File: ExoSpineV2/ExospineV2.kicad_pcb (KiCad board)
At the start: 2 copper layers, 79.2 x 75.6 mm, 51 parts, among them J1 GPIO, J11 JST PH 3pin, J12 2.54mm 4pin, J13 JST PH 5pin, J2 Screw Terminal 2pin 5mm, J21 JST PH 2pin, J22 JST PH 2pin, J23 JST PH 2pin, J3 Mounting Hole 2.7mm, J31 JST PH 3pin, J32 JST PH 3pin, J33 JST PH 3pin, J34 JST PH 3pin, J35 JST PH 3pin, J36 JST PH 3pin, J4 Mounting Hole 2.7mm, J5 Mounting Hole 2.7mm, J51 JST PH 2pin, J6 Mounting Hole 2.7mm, J61 JST PH 2pin, J71 JST PH 4pin, J72 JST PH 3pin, J73 JST PH 4pin, J74 JST PH 3pin, J75 JST PH 4pin, J76 JST PH 3pin, J77 JST PH 4pin, J78 JST PH 3pin, J81 JST PH 3pin, J82 JST PH 3pin, U1 MCP3008-I/SL, U2 74HC00D,653, U3 74HC00D,653

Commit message: little modifications
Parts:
- moved D1 5.30 mm to (117.3, 21.7)
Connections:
- J1 pad 12: /TemperatureSensors -> /Battery.NALCC
- J1 pad 7: /Battery.NALCC -> /TemperatureSensors
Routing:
- net Net-(J2-Pin_1): track 11.3 -> 0.00 mm
- net /Battery.NALCC: track 19.6 -> 28.6 mm
- net /Actuator2.Feedback: track 56.4 -> 61.0 mm, vias 0 -> 2
- net /TemperatureSensors: track 54.0 -> 52.4 mm
- added copper zone on B.Cu, net +5V
- added copper zone on F.Cu, net Net-(J2-Pin_1)

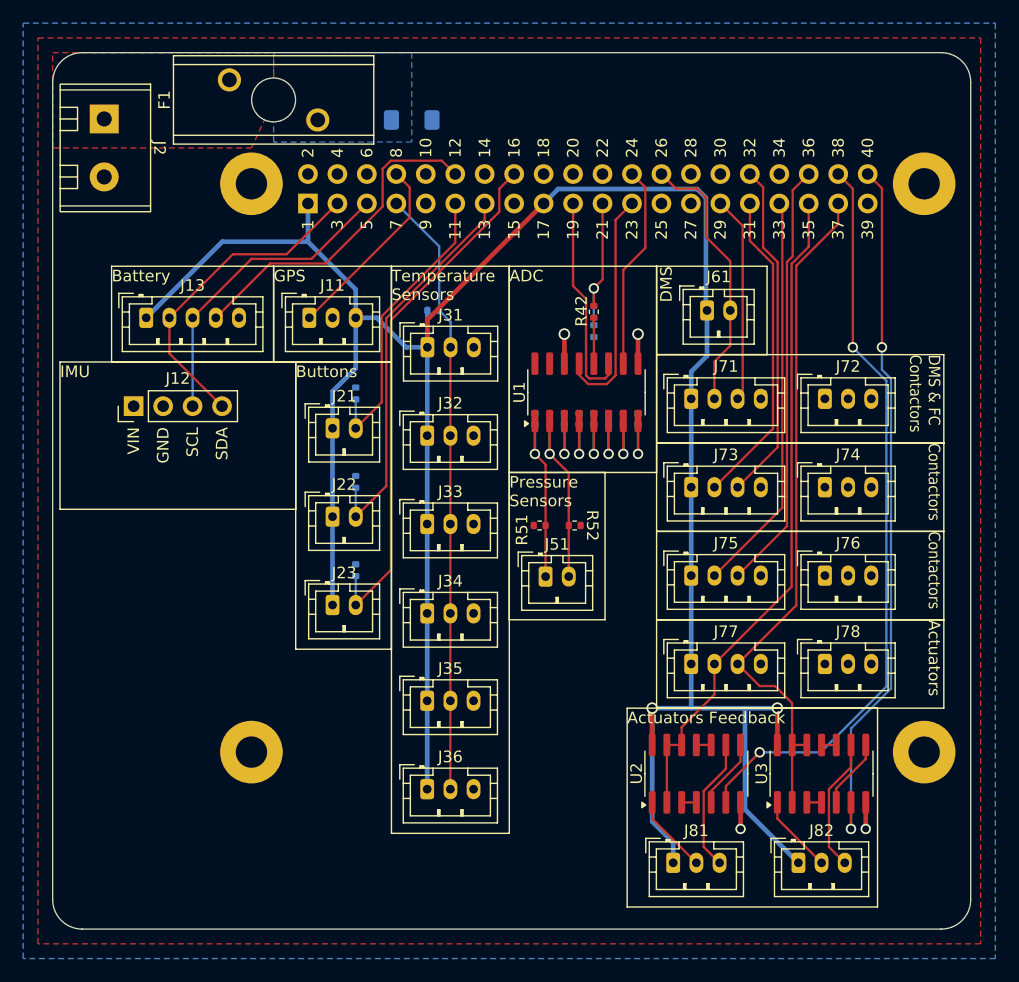
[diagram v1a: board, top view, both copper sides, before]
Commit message: chose all JLCPCB parts
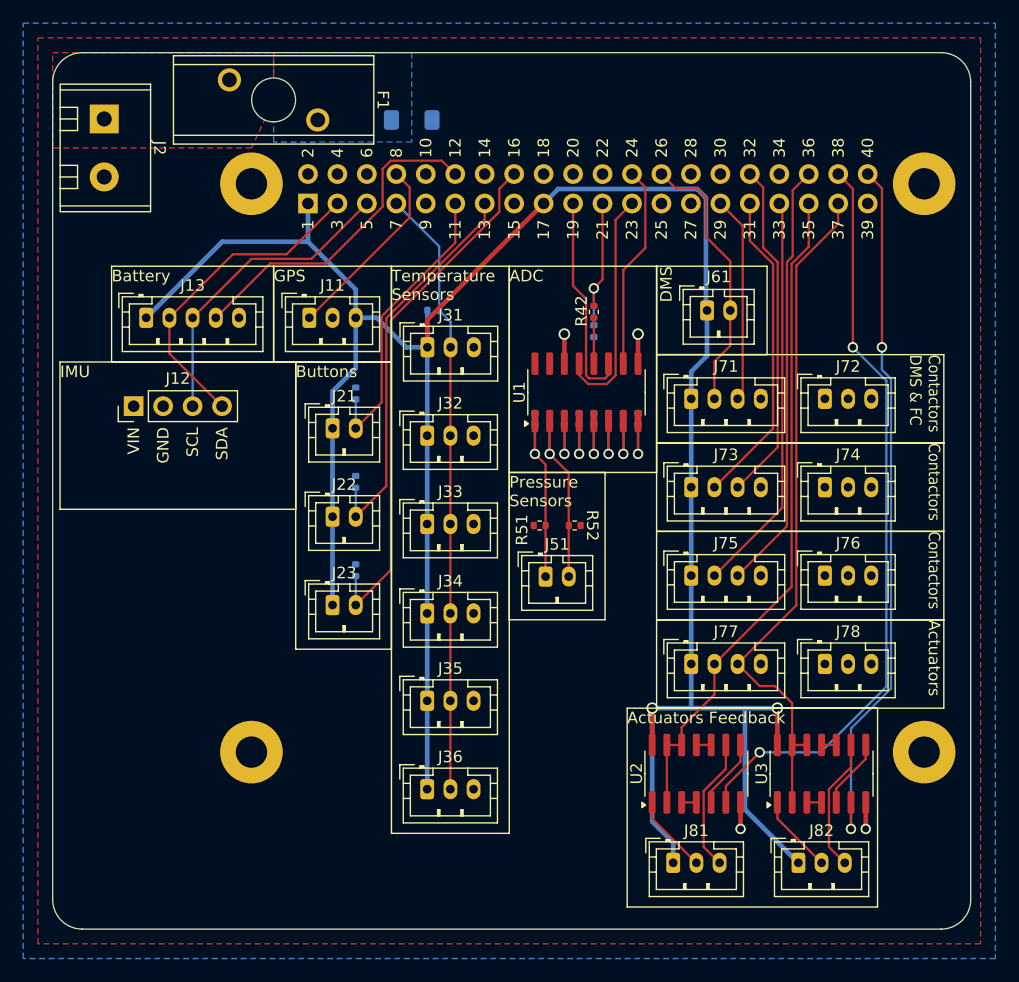
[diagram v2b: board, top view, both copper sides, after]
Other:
- board text added: "Contactors DMS & FC"
- board text removed: "DMS & FC Contactors"
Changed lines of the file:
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@@
 		(tags "Fuse")
 		(property "Reference" "F1"
-			(at 0 -8.83 90)
+			(at 0 8.84 270)
+			(unlocked yes)
 			(layer "F.SilkS")
 			(effects
@@
 		)
 	)
-	(gr_text "DMS & FC\nContactors"
+	(gr_text "Contactors\nDMS & FC"
 		(at 162.941 41.91 270)
 		(layer "F.SilkS")

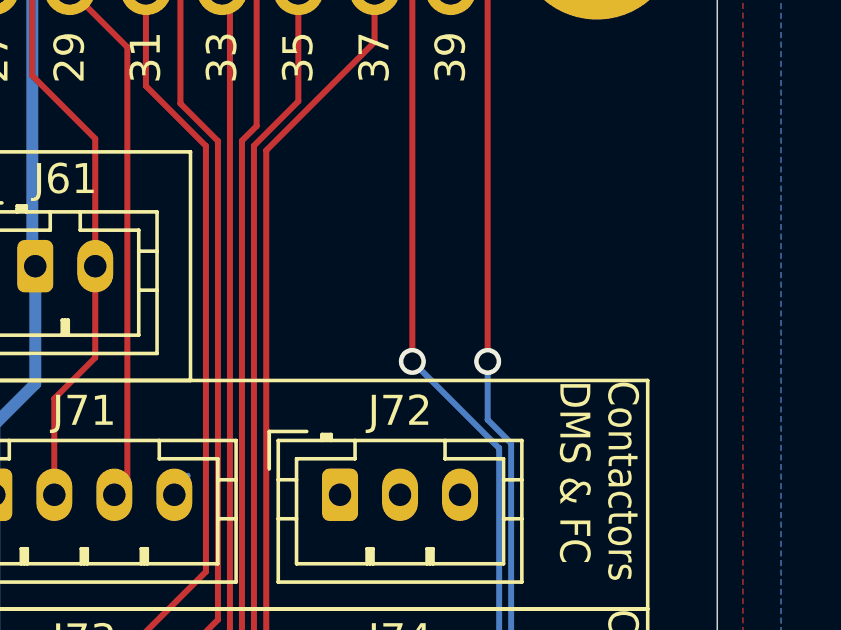
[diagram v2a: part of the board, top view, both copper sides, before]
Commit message: added resistors
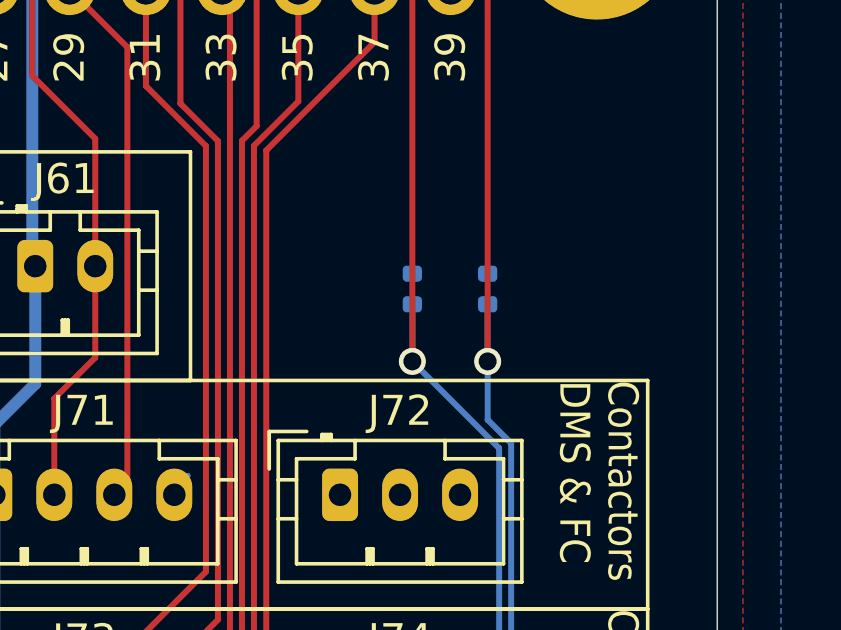
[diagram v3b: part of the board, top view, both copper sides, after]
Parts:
- added R81: 10k, Resistor_SMD:R_0402_1005Metric, B.Cu at (155.3, 38.9)
- added R82: 10k, Resistor_SMD:R_0402_1005Metric, B.Cu at (157.9, 38.9)
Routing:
- net /Actuator2.Feedback: track 61.0 -> 62.9 mm
- net /Actuator1.Feedback: track 64.7 -> 66.6 mm

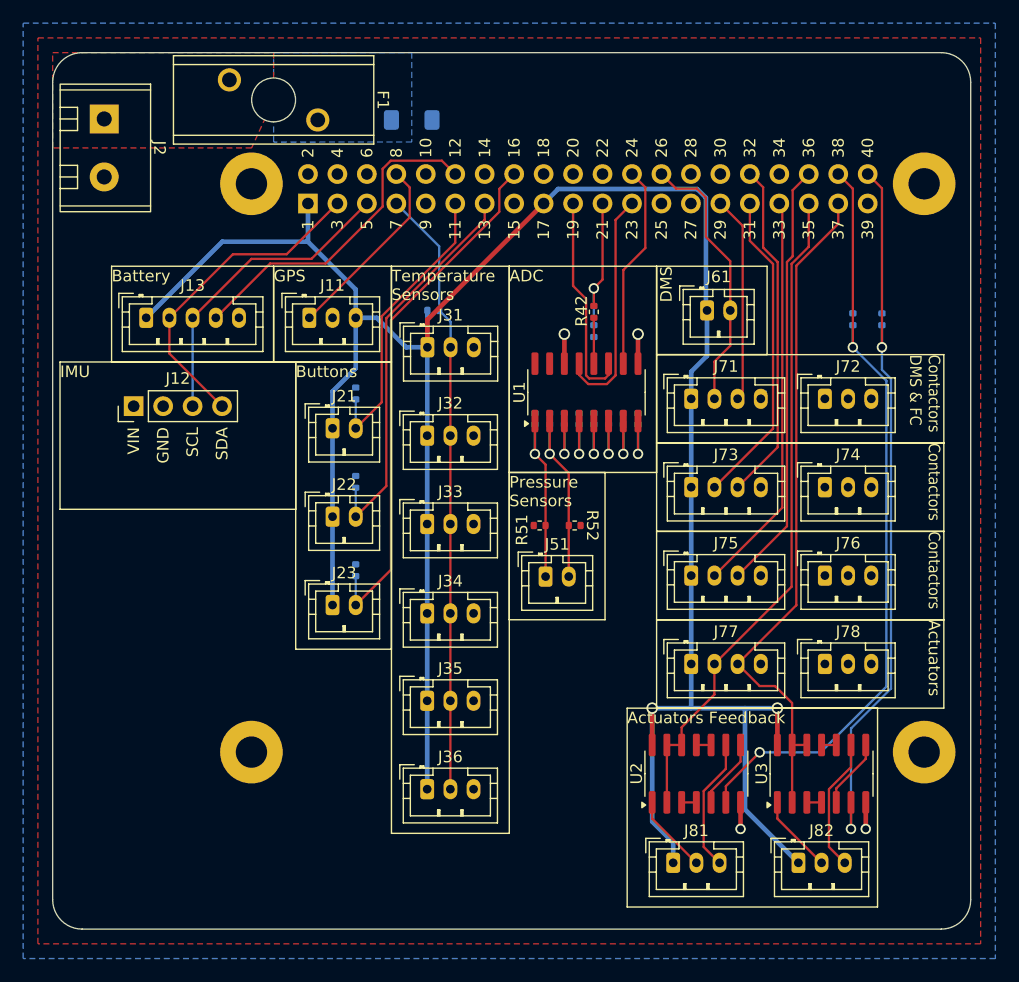
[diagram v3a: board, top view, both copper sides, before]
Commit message: added resistors for actuators feedback
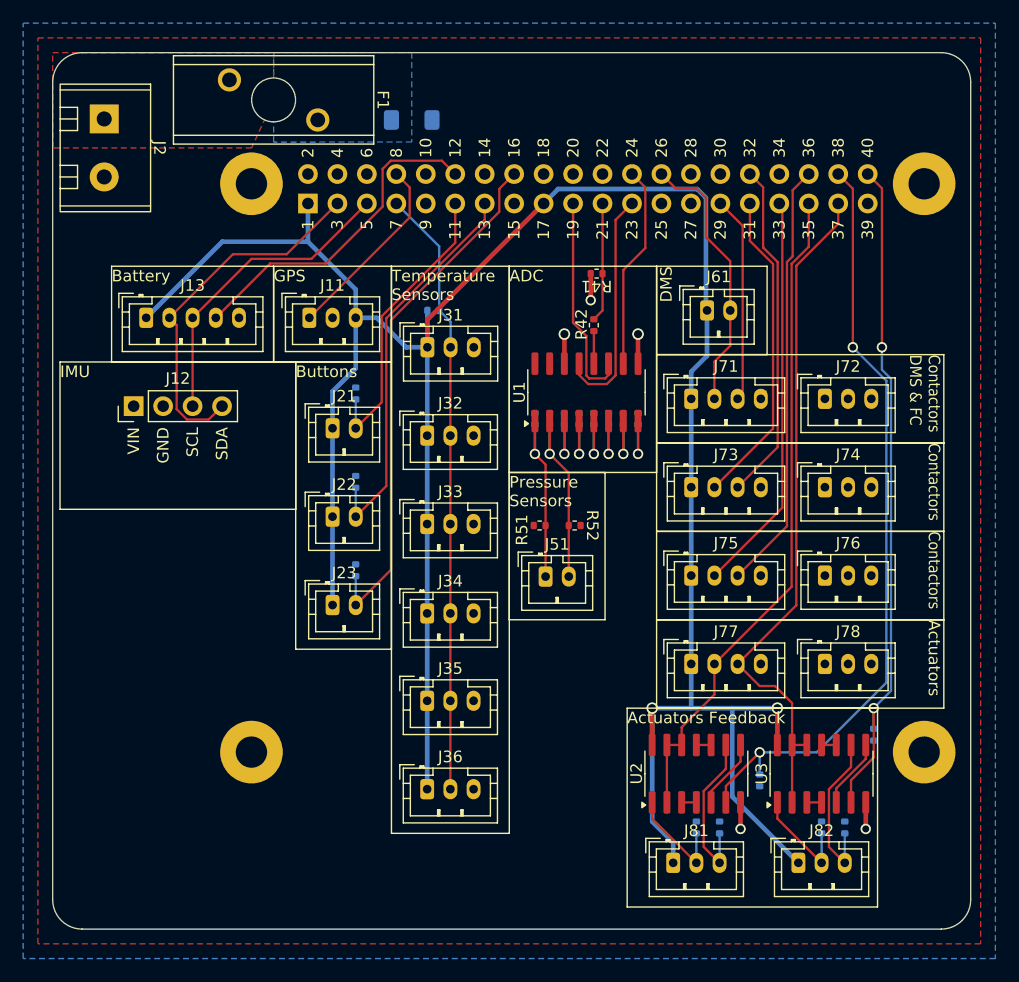
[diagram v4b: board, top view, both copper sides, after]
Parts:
- added R83: 10k, Resistor_SMD:R_0402_1005Metric, B.Cu at (152.7, 82.7)
- added R84: 10k, Resistor_SMD:R_0402_1005Metric, B.Cu at (154.7, 82.7)
- added R85: 10k, Resistor_SMD:R_0402_1005Metric, B.Cu at (147.3, 78.6)
- added R86: 10k, Resistor_SMD:R_0402_1005Metric, B.Cu at (157.2, 74.7)
- R41: moved to F.Cu
- moved R82 46.0 mm to (143.9, 82.7)
- moved R81 45.8 mm to (141.9, 82.7)
- moved R41 4.96 mm to (133.3, 34.9), turned to 0 degrees
- moved R42 1.14 mm to (133.0, 39.4)
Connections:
- J4 pad 1: GND -> unconnected-(J4-Pin_1-Pad1)
- J5 pad 1: GND -> unconnected-(J5-Pin_1-Pad1)
- R81 pad 1: /Actuator1.Feedback -> Net-(J81-Pin_2)
- R82 pad 1: /Actuator2.Feedback -> Net-(J81-Pin_3)
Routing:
- net /Actuator2.Feedback: track 62.9 -> 58.2 mm
- net /SDA: track 28.1 -> 31.5 mm
- net Net-(J82-Pin_2): track 6.79 -> 9.33 mm
- net Net-(J81-Pin_2): track 6.79 -> 9.33 mm
- net Net-(J82-Pin_3): track 11.5 -> 14.1 mm
- net Net-(J81-Pin_3): track 11.5 -> 14.1 mm
- net GND: track 10.3 -> 12.6 mm, vias 4 -> 5
- net /ADC.MISO: track 12.3 -> 10.3 mm, vias 1 -> 0
- net Net-(U1-Dout): track 3.95 -> 2.81 mm

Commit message: fixed errors
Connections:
- J4 pad 1: unconnected-(J4-Pin_1-Pad1) -> GND
- J5 pad 1: unconnected-(J5-Pin_1-Pad1) -> GND
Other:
- board text added: "Contactors (DMS)"
- board text removed: "Contactors DMS & FC"
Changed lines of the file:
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@@
 	(net 54 "Net-(J82-Pin_2)")
 	(net 55 "Net-(J2-Pin_1)")
-	(net 56 "unconnected-(J4-Pin_1-Pad1)")
-	(net 57 "unconnected-(J5-Pin_1-Pad1)")
 	(footprint "Connector_JST:JST_PH_B3B-PH-K_1x03_P2.00mm_Vertical"
 		(layer "F.Cu")
@@
 			(layers "*.Cu" "*.Mask")
 			(remove_unused_layers no)
-			(net 56 "unconnected-(J4-Pin_1-Pad1)")
+			(net 1 "GND")
 			(pinfunction "Pin_1")
 			(pintype "passive")
@@
 			(layers "*.Cu" "*.Mask")
 			(remove_unused_layers no)
-			(net 57 "unconnected-(J5-Pin_1-Pad1)")
+			(net 1 "GND")
 			(pinfunction "Pin_1")
 			(pintype "passive")
@@
 		)
 		(property "Value" "1k"
-			(at -0.0272 0.0002 360)
+			(at -0.0272 0.0002 0)
 			(layer "F.Fab")
 			(effects
@@
 		)
 		(fp_text user "${REFERENCE}"
-			(at 0 0 360)
+			(at 0 0 0)
 			(layer "F.Fab")
 			(effects
@@
 		(tags "resistor")
 		(property "Reference" "R84"
-			(at 0.92 0 270)
+			(at 0.92 0 -90)
 			(layer "B.SilkS")
 			(effects
@@
 		)
 		(property "Value" "10k"
-			(at 0 -1.17 270)
+			(at 0 -1.17 -90)
 			(layer "B.Fab")
 			(effects
@@
 		)
 		(fp_text user "${REFERENCE}"
-			(at 0 0 270)
+			(at 0 0 -90)
 			(layer "B.Fab")
 			(effects
@@
 		(tags "resistor")
 		(property "Reference" "R83"
-			(at 0.92 0 270)
+			(at 0.92 0 -90)
 			(layer "B.SilkS")
 			(effects
@@
 		)
 		(property "Value" "10k"
-			(at 0 -1.17 270)
+			(at 0 -1.17 -90)
 			(layer "B.Fab")
 			(effects
@@
 		)
 		(fp_text user "${REFERENCE}"
-			(at 0 0 270)
+			(at 0 0 -90)
 			(layer "B.Fab")
 			(effects
@@
 		(tags "resistor")
 		(property "Reference" "R81"
-			(at 0.92 0 270)
+			(at 0.92 0 -90)
 			(layer "B.SilkS")
 			(effects
@@
 		(tags "resistor")
 		(property "Reference" "R82"
-			(at 0.92 0 270)
+			(at 0.92 0 -90)
 			(layer "B.SilkS")
 			(effects
@@
 		)
 	)
-	(gr_text "Contactors\nDMS & FC"
+	(gr_text "Contactors\n(DMS)"
 		(at 162.941 41.91 270)
 		(layer "F.SilkS")
@@
 	(via
 		(at 145.669 82.804)
-		(size 0.9)
-		(drill 0.6)
+		(size 1.1)
+		(drill 0.8)
 		(layers "F.Cu" "B.Cu")
 		(free yes)
@@
 	(via
 		(at 156.464 82.804)
-		(size 0.9)
-		(drill 0.6)
+		(size 1.1)
+		(drill 0.8)
 		(layers "F.Cu" "B.Cu")
 		(free yes)
@@
 	(via
 		(at 132.75 37.22)
-		(size 0.9)
-		(drill 0.6)
+		(size 1.1)
+		(drill 0.8)
 		(layers "F.Cu" "B.Cu")
 		(free yes)
@@
 	(via
 		(at 130.48 40.14)
-		(size 1)
-		(drill 0.7)
+		(size 1.1)
+		(drill 0.8)
 		(layers "F.Cu" "B.Cu")
 		(net 1)
@@
 	(via
 		(at 136.83 40.14)
-		(size 1)
-		(drill 0.7)
+		(size 1.1)
+		(drill 0.8)
 		(layers "F.Cu" "B.Cu")
 		(net 1)
@@
 	(via
 		(at 157.15 72.39)
-		(size 0.9)
-		(drill 0.6)
+		(size 0.7)
+		(drill 0.4)
 		(layers "F.Cu" "B.Cu")
 		(free yes)
@@
 	(via
 		(at 157.86 41.275)
-		(size 0.9)
-		(drill 0.6)
+		(size 0.7)
+		(drill 0.4)
 		(layers "F.Cu" "B.Cu")
 		(free yes)
@@
 	(via
 		(at 147.32 76.2)
-		(size 0.9)
-		(drill 0.6)
+		(size 0.7)
+		(drill 0.4)
 		(layers "F.Cu" "B.Cu")
 		(net 8)
@@
 	(via
 		(at 155.35 41.275)
-		(size 0.9)
-		(drill 0.6)
+		(size 0.7)
+		(drill 0.4)
 		(layers "F.Cu" "B.Cu")
 		(free yes)
@@
 	(via
 		(at 148.844 72.39)
-		(size 1)
-		(drill 0.7)
+		(size 1.1)
+		(drill 0.8)
 		(layers "F.Cu" "B.Cu")
 		(net 32)
@@
 	(via
 		(at 138.049 72.39)
-		(size 1)
-		(drill 0.7)
+		(size 1.1)
+		(drill 0.8)
 		(layers "F.Cu" "B.Cu")
 		(net 32)
@@
 	(via
 		(at 129.21 50.47)
-		(size 0.9)
-		(drill 0.6)
+		(size 0.7)
+		(drill 0.4)
 		(layers "F.Cu" "B.Cu")
 		(net 33)
@@
 	(via
 		(at 130.48 50.47)
-		(size 0.9)
-		(drill 0.6)
+		(size 0.7)
+		(drill 0.4)
 		(layers "F.Cu" "B.Cu")
 		(net 34)
@@
 	(via
 		(at 131.75 50.47)
-		(size 0.9)
-		(drill 0.6)
+		(size 0.7)
+		(drill 0.4)
 		(layers "F.Cu" "B.Cu")
 		(net 35)
@@
 	(via
 		(at 133.02 50.47)
-		(size 0.9)
-		(drill 0.6)
+		(size 0.7)
+		(drill 0.4)
 		(layers "F.Cu" "B.Cu")
 		(net 36)
@@
 	(via
 		(at 134.29 50.47)
-		(size 0.9)
-		(drill 0.6)
+		(size 0.7)
+		(drill 0.4)
 		(layers "F.Cu" "B.Cu")
 		(net 37)
@@
 	(via
 		(at 135.56 50.47)
-		(size 0.9)
-		(drill 0.6)
+		(size 0.7)
+		(drill 0.4)
 		(layers "F.Cu" "B.Cu")
 		(net 38)
@@
 	(via
 		(at 127.94 50.47)
-		(size 0.9)
-		(drill 0.6)
+		(size 0.7)
+		(drill 0.4)
 		(layers "F.Cu" "B.Cu")
 		(net 39)
@@
 	(via
 		(at 136.83 50.47)
-		(size 0.9)
-		(drill 0.6)
+		(size 0.7)
+		(drill 0.4)
 		(layers "F.Cu" "B.Cu")
 		(net 40)

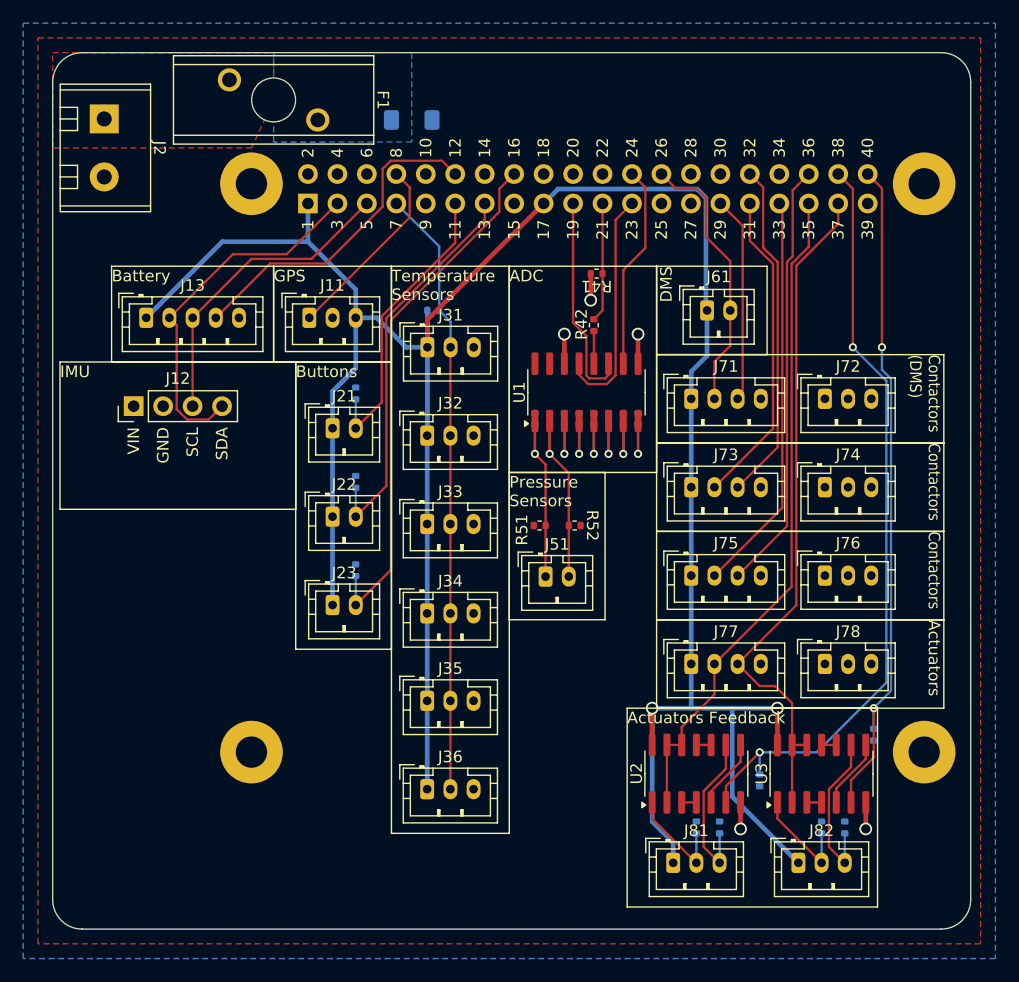
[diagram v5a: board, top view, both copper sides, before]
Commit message: added graphics
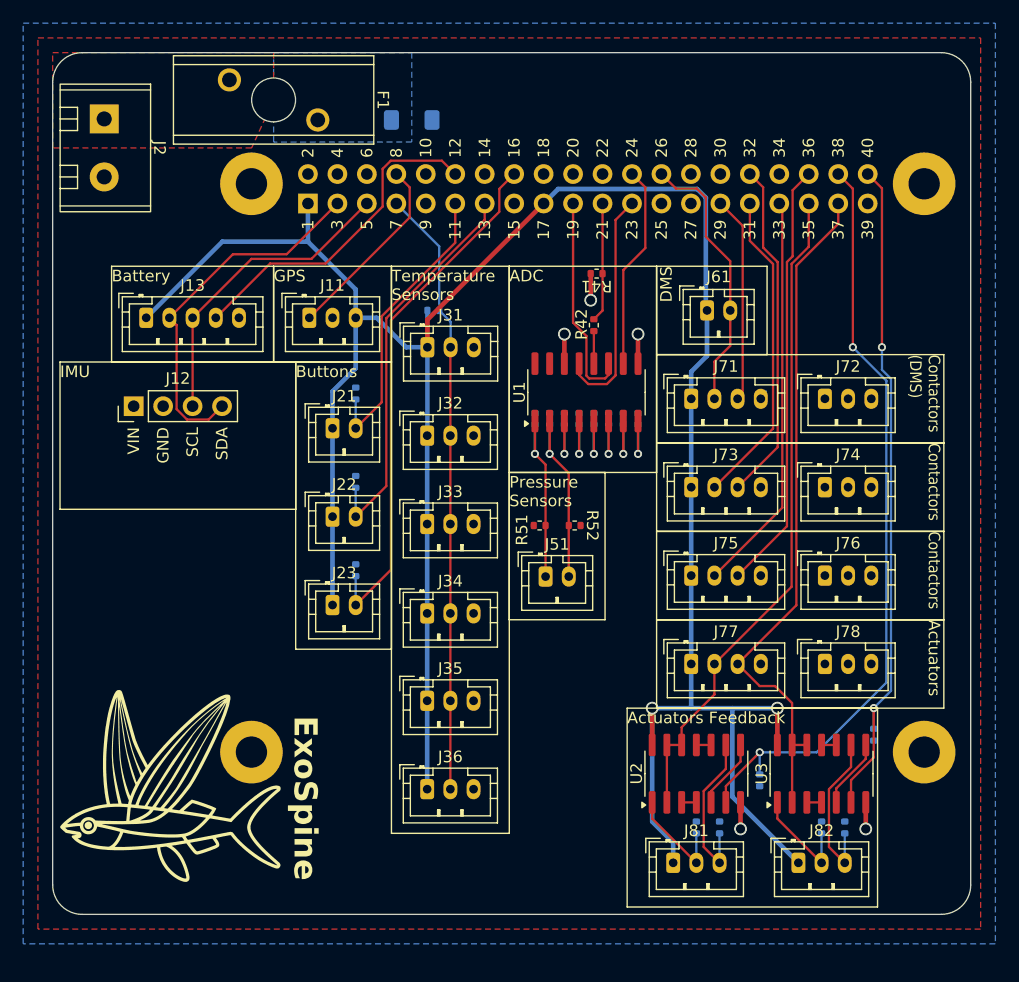
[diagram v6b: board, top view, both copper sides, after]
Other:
- board size 79.2 x 75.6 mm -> 79.2 x 74.3 mm
- board text added: "ExoSpine"
